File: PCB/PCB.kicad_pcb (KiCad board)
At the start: 2 copper layers, 419.1 x 97.6 mm, 201 parts, among them J1 USB_mini_micro_B, K0,0 KEYSW, K0,1 KEYSW, K0,10 KEYSW, K0,11 KEYSW, K0,12 KEYSW, K0,13 KEYSW, K0,14 KEYSW, K0,15 KEYSW, K0,16 KEYSW, K0,17 KEYSW, K0,18 KEYSW, K0,19 KEYSW, K0,2 KEYSW, K0,20 KEYSW, K0,3 KEYSW, K0,4 KEYSW, K0,5 KEYSW, K0,6 KEYSW, K0,7 KEYSW, K0,8 KEYSW, K0,9 KEYSW, K1,0 KEYSW, K1,1 KEYSW, K1,10 KEYSW, K1,11 KEYSW, K1,12 KEYSW, K1,13 KEYSW, K1,14 KEYSW, K1,15 KEYSW, K1,16 KEYSW, K1,17 KEYSW, K1,18 KEYSW, K1,19 KEYSW, K1,2 KEYSW, K1,20 KEYSW, K1,3 KEYSW, K1,4 KEYSW, K1,5 KEYSW, K1,6 KEYSW, K1,7 KEYSW, K1,8 KEYSW, K1,9 KEYSW, K2,0 KEYSW, K2,1 KEYSW, K2,10 KEYSW, K2,11 KEYSW, K2,12 KEYSW, K2,13 KEYSW, K2,14 KEYSW, K2,15 KEYSW, K2,17 KEYSW, K2,18 KEYSW, K2,19 KEYSW, K2,2 KEYSW, K2,20 KEYSW, K2,4 KEYSW, K2,5 KEYSW, K2,6 KEYSW, K2,7 KEYSW, K2,8 KEYSW, K2,9 KEYSW, K3,0 KEYSW, K3,1 KEYSW, K3,10 KEYSW, K3,11 KEYSW, K3,12 KEYSW, K3,13 KEYSW, K3,14 KEYSW, K3,16 KEYSW, K3,18 KEYSW, K3,19 KEYSW, K3,2 KEYSW, K3,20 KEYSW, K3,3 KEYSW, K3,4 KEYSW, K3,5 KEYSW, K3,6 KEYSW, K3,7 KEYSW, K3,8 KEYSW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

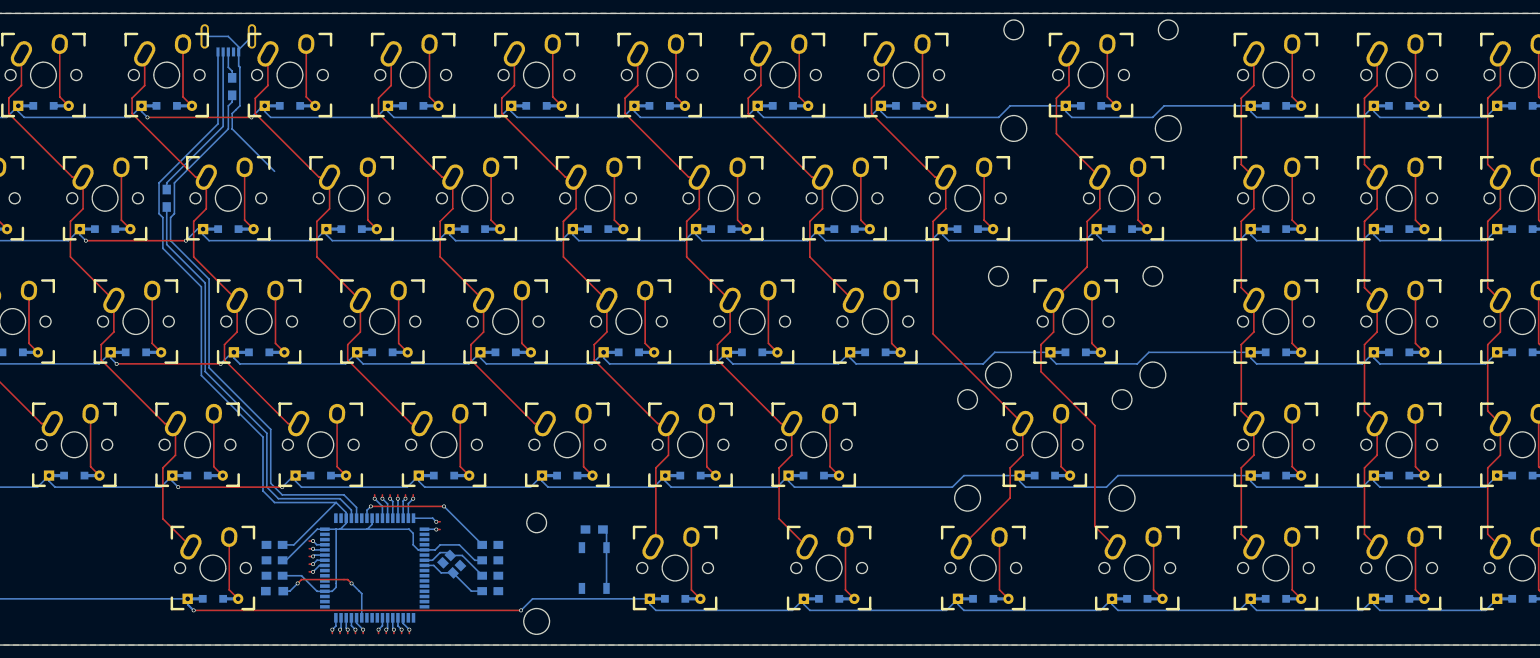
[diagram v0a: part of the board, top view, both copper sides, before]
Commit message: Connected many columns
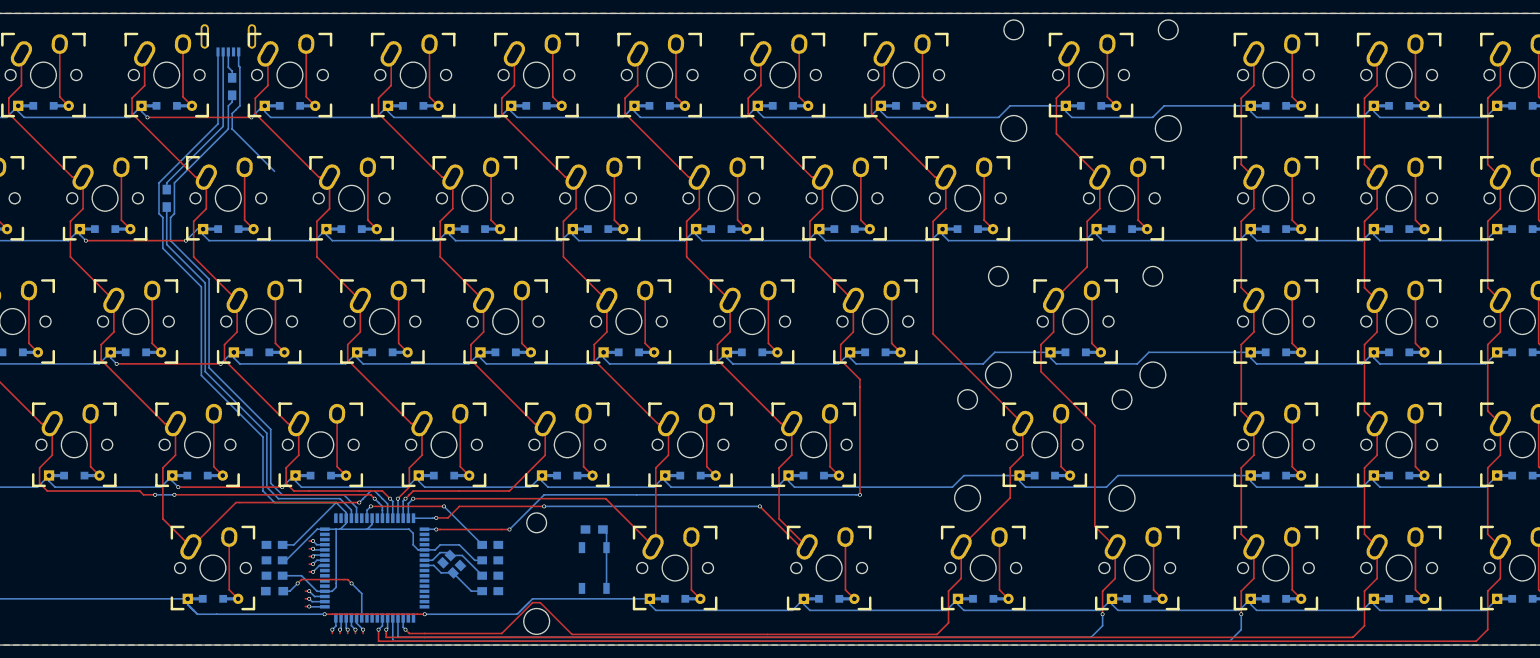
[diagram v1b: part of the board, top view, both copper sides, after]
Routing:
- net /col20: track 85.3 -> 272.3 mm
- net /col19: track 85.2 -> 250.7 mm
- net /col18: track 85.2 -> 231.7 mm
- net /col17: track 91.0 -> 214.0 mm
- net /col16: track 96.0 -> 196.7 mm
- net /col15: track 50.7 -> 149.9 mm, vias 1 -> 3
- net /col8: track 77.9 -> 140.1 mm, vias 1 -> 3
- net /col14: track 100.9 -> 159.6 mm, vias 1 -> 3
- net /col13: track 97.9 -> 137.4 mm
- net /col9: track 99.5 -> 132.6 mm
- net /col12: track 77.6 -> 106.2 mm
- net /col10: track 77.6 -> 104.1 mm
- net /col11: track 77.9 -> 90.4 mm
- net GND: track 31.7 -> 22.1 mm
- net /row4: track 419.8 -> 424.5 mm
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
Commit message: All rows and columns connected
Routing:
- net /col0: track 90.9 -> 316.2 mm
- net /col1: track 65.2 -> 288.5 mm, vias 1 -> 3
- net /col2: track 85.7 -> 280.4 mm, vias 1 -> 3
- net /col3: track 91.3 -> 259.8 mm, vias 1 -> 0
- net /col4: track 92.4 -> 245.4 mm, vias 1 -> 0
- net /col5: track 103.7 -> 233.4 mm, vias 1 -> 0
- net /col6: track 100.5 -> 206.2 mm
- net /col7: track 76.6 -> 168.3 mm, vias 1 -> 3
- net /row0: track 442.4 -> 519.7 mm, vias 3 -> 4
- net /row1: track 441.7 -> 513.6 mm, vias 3 -> 4
- net /row2: track 438.3 -> 491.4 mm, vias 3 -> 4
- net /row3: track 437.9 -> 463.1 mm, vias 3 -> 4
- net /row4: track 424.5 -> 434.7 mm, vias 3 -> 5
- net /col20: track 272.3 -> 271.3 mm
- net /col19: track 250.7 -> 250.0 mm
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
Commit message: Started cleanup of routes and vias
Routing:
- net GND: track 22.1 -> 106.0 mm, vias 0 -> 4
- net VCC: track 164.1 -> 214.6 mm, vias 0 -> 6
- net /row2: track 491.4 -> 450.7 mm, vias 4 -> 1
- net Net-(RR1-Pad1): track 9.33 -> 41.3 mm
- net /col20: track 271.3 -> 267.3 mm
- net /col18: track 231.0 -> 227.1 mm, vias 1 -> 0
- net /col17: track 213.3 -> 209.8 mm, vias 1 -> 0
- net /col16: track 196.7 -> 193.3 mm
- net /col19: track 250.0 -> 246.7 mm
- net /col7: track 168.3 -> 165.1 mm
- net /col6: track 206.2 -> 209.1 mm, vias 1 -> 0
- net /row1: track 513.6 -> 511.0 mm, vias 4 -> 0
- net /row3: track 463.1 -> 465.0 mm, vias 4 -> 0
- net /col14: track 159.6 -> 161.4 mm, vias 3 -> 1
- net Net-(RR2-Pad2): track 17.5 -> 19.1 mm
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
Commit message: More routing cleanup
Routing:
- net /row2: track 450.7 -> 436.0 mm, vias 1 -> 0
- net /col2: track 280.3 -> 277.3 mm, vias 3 -> 1
- net /col0: track 315.1 -> 312.6 mm
- net /col1: track 287.6 -> 285.9 mm, vias 3 -> 2
- net VCC: track 214.6 -> 213.7 mm
- net /row4: track 435.4 -> 434.6 mm

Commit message: Redid the layout to resemble the Teensy++ 2.0 more
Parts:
- removed C5: 0.1u, Capacitors_SMD:C_0805_HandSoldering
- removed C6: 4.7u, Capacitors_SMD:C_0805_HandSoldering
- added CA1: 0.1u, Capacitors_SMD:C_0805_HandSoldering, B.Cu at (308.4, 237.5)
- added CX1: 10p, Capacitors_SMD:C_0805_HandSoldering, B.Cu at (342.9, 242.3)
- added CX2: 10p, Capacitors_SMD:C_0805_HandSoldering, B.Cu at (342.9, 239.9)
- C1, C2: value 22p -> 0.1u
- C4: value 0.1u -> 1u
- RR2: value 10k -> 1k
- X1: value XTAL_GND -> 16M; footprint Crystals:crystal_FA238-TSX3225 -> keyboard_parts:FA-238
- moved C2 35.1 mm to (308.4, 230.4), turned to 180 degrees
- moved CU1 34.7 mm to (308.4, 235.1), turned to 180 degrees
- moved C3 34.6 mm to (308.4, 232.8), turned to 180 degrees
- moved RR1 18.0 mm to (341.1, 227.4)
- moved SW1 17.9 mm to (341.1, 234.0), turned to 0 degrees
- moved C1 9.69 mm to (341.1, 229.8)
- moved X1 6.07 mm to (338.1, 241.1), turned to 90 degrees
- moved C4 3.21 mm to (308.4, 239.9)
- moved RR2 3.21 mm to (308.4, 242.3)
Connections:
- C1 pad 1: Net-(C1-Pad1) -> VCC
- C2 pad 1: Net-(C2-Pad1) -> VCC
- J1 pad 4: Net-(J1-Pad4) -> (no net)
- U1 pad 1: Net-(U1-Pad1) -> (no net)
- U1 pad 18: Net-(U1-Pad18) -> (no net)
- U1 pad 19: Net-(U1-Pad19) -> (no net)
- U1 pad 2: Net-(U1-Pad2) -> (no net)
- U1 pad 23: Net-(C2-Pad1) -> Net-(CX2-Pad1)
- U1 pad 24: Net-(C1-Pad1) -> Net-(CX1-Pad1)
- U1 pad 25: Net-(U1-Pad25) -> (no net)
- U1 pad 26: Net-(U1-Pad26) -> (no net)
- U1 pad 27: Net-(U1-Pad27) -> (no net)
- U1 pad 28: Net-(U1-Pad28) -> (no net)
- U1 pad 29: Net-(U1-Pad29) -> (no net)
- U1 pad 30: Net-(U1-Pad30) -> (no net)
- U1 pad 31: Net-(U1-Pad31) -> (no net)
- U1 pad 32: Net-(U1-Pad32) -> (no net)
- U1 pad 33: Net-(U1-Pad33) -> (no net)
- U1 pad 34: Net-(U1-Pad34) -> (no net)
- U1 pad 40: Net-(U1-Pad40) -> (no net)
- U1 pad 41: Net-(U1-Pad41) -> (no net)
- U1 pad 42: Net-(U1-Pad42) -> (no net)
- U1 pad 54: Net-(U1-Pad54) -> (no net)
- U1 pad 55: Net-(U1-Pad55) -> (no net)
- U1 pad 56: Net-(U1-Pad56) -> (no net)
- U1 pad 9: Net-(U1-Pad9) -> (no net)
- X1 pad 1: Net-(C1-Pad1) -> Net-(CX1-Pad1)
- X1 pad 2: Net-(C2-Pad1) -> Net-(CX2-Pad1)
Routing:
- net /row2: track 436.0 -> 475.6 mm, vias 0 -> 2
- net VCC: track 213.7 -> 182.7 mm
- net Net-(CA1-Pad1): track 0.00 -> 19.7 mm, vias 0 -> 2
- net Net-(RR1-Pad1): track 41.3 -> 24.3 mm
- net GND: track 105.9 -> 122.4 mm, vias 4 -> 3
- net Net-(CX1-Pad1): track 0.00 -> 15.1 mm
- net Net-(CX2-Pad1): track 0.00 -> 11.5 mm
- net Net-(C1-Pad1): track 11.2 -> 0.00 mm
- net Net-(C2-Pad1): track 10.9 -> 0.00 mm
- net Net-(CU1-Pad1): track 20.3 -> 18.5 mm
- net Net-(RR2-Pad2): track 19.1 -> 18.1 mm

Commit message: Taking new design approach; updated submodules
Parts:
- removed C1, C2, C3, CA1: 0.1u, Capacitors_SMD:C_0805_HandSoldering
- removed C4, CU1: 1u, Capacitors_SMD:C_0805_HandSoldering
- removed CX1, CX2: 10p, Capacitors_SMD:C_0805_HandSoldering
- removed J1: USB_mini_micro_B, keyboard_parts:USB_miniB_hirose_5S8
- removed RR1: 10k, Resistors_SMD:R_0805_HandSoldering
- removed RR2: 1k, Resistors_SMD:R_0805_HandSoldering
- removed RU1, RU2: 22, Resistors_SMD:R_0805_HandSoldering
- removed SW1: SW_PUSH, Buttons_Switches_SMD:SW_SPST_TL3342
- removed X1: 16M, keyboard_parts:FA-238
- U1: value AT90USB1286 -> Teensy2.0++; footprint Housings_QFP:TQFP-64_14x14mm_Pitch0.8mm -> keebs:Teensy_20
- moved U1 66.2 mm to (372.6, 281.8)
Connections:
- U1 pad 1: (no net) -> /col15
- U1 pad 10: /col8 -> (no net)
- U1 pad 11: /col9 -> (no net)
- U1 pad 12: /col10 -> (no net)
- U1 pad 13: /col11 -> /row0
- U1 pad 14: /col12 -> /row1
- U1 pad 15: /col13 -> /row2
- U1 pad 16: /col14 -> /row3
- U1 pad 17: /col15 -> /row4
- U1 pad 20: Net-(RR1-Pad1) -> (no net)
- U1 pad 21: VCC -> /col0
- U1 pad 22: GND -> /col1
- U1 pad 23: Net-(CX2-Pad1) -> /col2
- U1 pad 24: Net-(CX1-Pad1) -> /col3
- U1 pad 25: (no net) -> /col4
- U1 pad 26: (no net) -> /col5
- U1 pad 27: (no net) -> /col6
- U1 pad 28: (no net) -> /col7
- U1 pad 3: VCC -> /col16
- U1 pad 4: Net-(RU1-Pad1) -> /col17
- U1 pad 5: Net-(RU2-Pad1) -> /col18
- U1 pad 6: GND -> /col19
- U1 pad 7: Net-(CU1-Pad1) -> /col20
- U1 pad 8: VCC -> (no net)
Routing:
- net (no net): track 0.00 -> 591.9 mm, vias 0 -> 15
- net VCC: track 182.7 -> 0.00 mm, vias 6 -> 0
- net GND: track 122.4 -> 0.00 mm, vias 3 -> 0
- net Net-(RU2-Pad1): track 85.6 -> 0.00 mm
- net Net-(RU1-Pad1): track 64.8 -> 0.00 mm
- net Net-(J1-Pad2): track 24.9 -> 0.00 mm
- net Net-(RR1-Pad1): track 24.3 -> 0.00 mm
- net Net-(CA1-Pad1): track 19.7 -> 0.00 mm, vias 2 -> 0
- net Net-(CU1-Pad1): track 18.5 -> 0.00 mm, vias 2 -> 0
- net Net-(RR2-Pad2): track 18.1 -> 0.00 mm, vias 2 -> 0
- net Net-(CX1-Pad1): track 15.1 -> 0.00 mm
- net Net-(CX2-Pad1): track 11.5 -> 0.00 mm
- net Net-(J1-Pad3): track 4.25 -> 0.00 mm

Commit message: 2017.11.08 Update
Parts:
- removed U1: Teensy2.0++, keebs:Teensy_20
- moved D4,9 135.9 mm to (257.0, 111.6), turned to 90 degrees
- moved D0,10 133.7 mm to (240.8, 41.1)
- moved D0,11 133.7 mm to (259.9, 41.1)
- moved D0,16 133.7 mm to (355.1, 41.1)
- moved D0,2 133.7 mm to (88.4, 41.1)
- moved D0,20 133.7 mm to (450.4, 41.1)
- moved D0,5 133.7 mm to (145.6, 41.1)
- moved D1,13 133.7 mm to (307.5, 60.2)
- moved D1,2 133.7 mm to (88.4, 60.2)
- moved D1,20 133.7 mm to (450.4, 60.2)
- moved D1,7 133.7 mm to (193.2, 60.2)
- moved D1,8 133.7 mm to (212.2, 60.2)
- moved D2,14 133.7 mm to (331.3, 79.2)
- moved D2,2 133.7 mm to (88.4, 79.2)
- moved D2,20 133.7 mm to (450.4, 79.2)
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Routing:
- net (no net): track 591.9 -> 0.00 mm, vias 15 -> 0
- net /col0: track 312.6 -> 87.6 mm, vias 1 -> 0
- net /col1: track 285.9 -> 62.0 mm, vias 2 -> 0
- net /col2: track 277.3 -> 82.7 mm, vias 1 -> 0
- net /col20: track 267.3 -> 82.7 mm, vias 1 -> 0
- net /col3: track 260.3 -> 88.2 mm
- net /row4: track 434.6 -> 267.8 mm, vias 3 -> 0
- net /col19: track 246.7 -> 82.7 mm, vias 1 -> 0
- net /col4: track 246.4 -> 91.1 mm
- net /col18: track 227.1 -> 82.7 mm
- net /col5: track 234.9 -> 101.2 mm
- net /col17: track 209.8 -> 88.3 mm
- net /col6: track 209.1 -> 98.6 mm
- net /col15: track 148.4 -> 48.2 mm, vias 1 -> 0
- net /col16: track 193.3 -> 93.2 mm, vias 1 -> 0
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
